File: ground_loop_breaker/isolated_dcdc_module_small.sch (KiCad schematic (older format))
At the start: 18 parts, among them J7 Conn_01x02_Male, J8 Conn_Coaxial, J9 Conn_01x02_Male

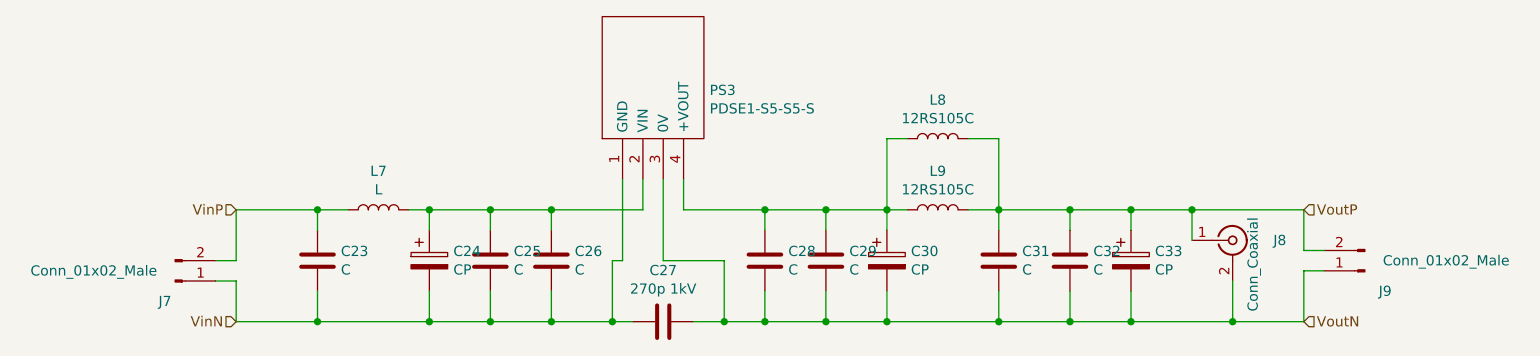
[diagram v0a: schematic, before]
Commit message: ground loop breaker fin
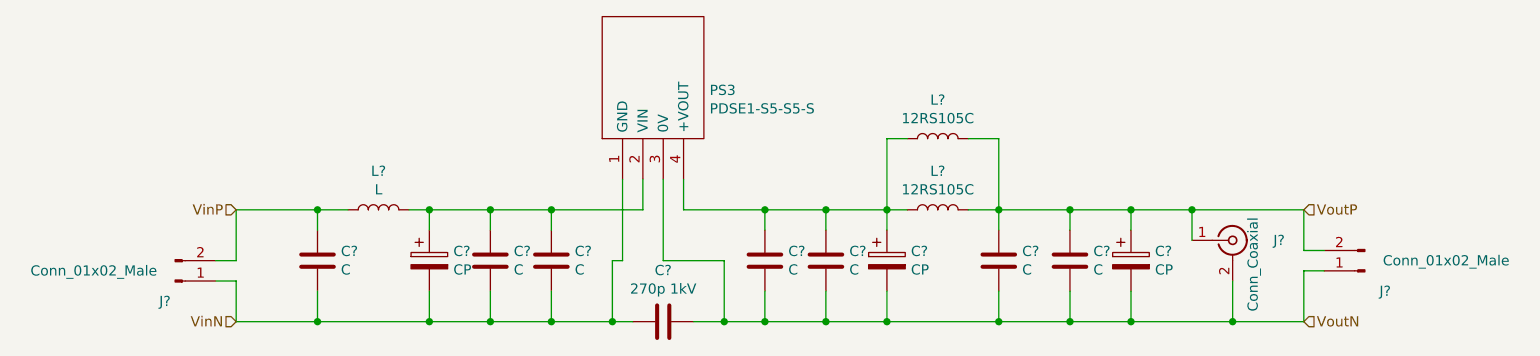
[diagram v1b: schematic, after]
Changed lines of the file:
@@
 $Descr A4 11693 8268
 encoding utf-8
-Sheet 4 5
+Sheet 3 5
 Title ""
 Date ""
@@
 AR Path="/613A5306/613A68CE" Ref="C26"  Part="1"
 AR Path="/613C5D0D/613A68CE" Ref="C?"  Part="1"
-F 0 "C26" H 4015 4146 50  0000 L CNN
+AR Path="/6135BAF1/613A68CE" Ref="C48"  Part="1"
+AR Path="/6135EEFA/613A68CE" Ref="C48"  Part="1"
+AR Path="/61365BC4/613A68CE" Ref="C?"  Part="1"
+F 0 "C?" H 4015 4146 50  0000 L CNN
 F 1 "C" H 4015 4055 50  0000 L CNN
 F 2 "SamacSys_Parts:C_1206_0805_dual" H 3938 3950 50  0001 C CNN
@@
 AR Path="/613A5306/613A68D4" Ref="C25"  Part="1"
 AR Path="/613C5D0D/613A68D4" Ref="C?"  Part="1"
-F 0 "C25" H 3715 4146 50  0000 L CNN
+AR Path="/6135BAF1/613A68D4" Ref="C47"  Part="1"
+AR Path="/6135EEFA/613A68D4" Ref="C47"  Part="1"
+AR Path="/61365BC4/613A68D4" Ref="C?"  Part="1"
+F 0 "C?" H 3715 4146 50  0000 L CNN
 F 1 "C" H 3715 4055 50  0000 L CNN
 F 2 "Capacitor_SMD:C_1206_3216Metric_Pad1.42x1.75mm_HandSolder" H 3638 3950 50  0001 C CNN
@@
 AR Path="/613A5306/613A68E2" Ref="C24"  Part="1"
 AR Path="/613C5D0D/613A68E2" Ref="C?"  Part="1"
-F 0 "C24" H 3418 4146 50  0000 L CNN
+AR Path="/6135BAF1/613A68E2" Ref="C46"  Part="1"
+AR Path="/6135EEFA/613A68E2" Ref="C46"  Part="1"
+AR Path="/61365BC4/613A68E2" Ref="C?"  Part="1"
+F 0 "C?" H 3418 4146 50  0000 L CNN
 F 1 "CP" H 3418 4055 50  0000 L CNN
 F 2 "SamacSys_Parts:CP_Radial_D8_P3.5_2.5" H 3338 3950 50  0001 C CNN
@@
 AR Path="/613A5306/613A68F0" Ref="C23"  Part="1"
 AR Path="/613C5D0D/613A68F0" Ref="C?"  Part="1"
-F 0 "C23" H 2865 4146 50  0000 L CNN
+AR Path="/6135BAF1/613A68F0" Ref="C45"  Part="1"
+AR Path="/6135EEFA/613A68F0" Ref="C45"  Part="1"
+AR Path="/61365BC4/613A68F0" Ref="C?"  Part="1"
+F 0 "C?" H 2865 4146 50  0000 L CNN
 F 1 "C" H 2865 4055 50  0000 L CNN
 F 2 "Capacitor_SMD:C_1206_3216Metric_Pad1.42x1.75mm_HandSolder" H 2788 3950 50  0001 C CNN
@@
 AR Path="/613A5306/613A68F6" Ref="L7"  Part="1"
 AR Path="/613C5D0D/613A68F6" Ref="L?"  Part="1"
-F 0 "L7" V 3240 3850 50  0000 C CNN
+AR Path="/6135BAF1/613A68F6" Ref="L13"  Part="1"
+AR Path="/6135EEFA/613A68F6" Ref="L13"  Part="1"
+AR Path="/61365BC4/613A68F6" Ref="L?"  Part="1"
+F 0 "L?" V 3240 3850 50  0000 C CNN
 F 1 "L" V 3149 3850 50  0000 C CNN
 F 2 "Inductor_SMD:L_Bourns-SRN4018" H 3050 3850 50  0001 C CNN
@@
 AR Path="/613A5306/613A68FF" Ref="C29"  Part="1"
 AR Path="/613C5D0D/613A68FF" Ref="C?"  Part="1"
-F 0 "C29" H 5365 4146 50  0000 L CNN
+AR Path="/6135BAF1/613A68FF" Ref="C51"  Part="1"
+AR Path="/6135EEFA/613A68FF" Ref="C51"  Part="1"
+AR Path="/61365BC4/613A68FF" Ref="C?"  Part="1"
+F 0 "C?" H 5365 4146 50  0000 L CNN
 F 1 "C" H 5365 4055 50  0000 L CNN
 F 2 "Capacitor_SMD:C_1206_3216Metric_Pad1.42x1.75mm_HandSolder" H 5288 3950 50  0001 C CNN
@@
 AR Path="/613A5306/613A6915" Ref="C31"  Part="1"
 AR Path="/613C5D0D/613A6915" Ref="C?"  Part="1"
-F 0 "C31" H 6215 4146 50  0000 L CNN
+AR Path="/6135BAF1/613A6915" Ref="C53"  Part="1"
+AR Path="/6135EEFA/613A6915" Ref="C53"  Part="1"
+AR Path="/61365BC4/613A6915" Ref="C?"  Part="1"
+F 0 "C?" H 6215 4146 50  0000 L CNN
 F 1 "C" H 6215 4055 50  0000 L CNN
 F 2 "Capacitor_SMD:C_1206_3216Metric_Pad1.42x1.75mm_HandSolder" H 6138 3950 50  0001 C CNN
@@
 AR Path="/613A5306/613A691B" Ref="L9"  Part="1"
 AR Path="/613C5D0D/613A691B" Ref="L?"  Part="1"
-F 0 "L9" V 5990 3850 50  0000 C CNN
+AR Path="/6135BAF1/613A691B" Ref="L15"  Part="1"
+AR Path="/6135EEFA/613A691B" Ref="L15"  Part="1"
+AR Path="/61365BC4/613A691B" Ref="L?"  Part="1"
+F 0 "L?" V 5990 3850 50  0000 C CNN
 F 1 "12RS105C" V 5899 3850 50  0000 C CNN
 F 2 "Inductor_THT:L_Radial_D10.5mm_P4.00x5.00mm_Murata_1200RS" H 5800 3850 50  0001 C CNN
@@
 AR Path="/613A5306/613A6922" Ref="C28"  Part="1"
 AR Path="/613C5D0D/613A6922" Ref="C?"  Part="1"
-F 0 "C28" H 5065 4146 50  0000 L CNN
+AR Path="/6135BAF1/613A6922" Ref="C50"  Part="1"
+AR Path="/6135EEFA/613A6922" Ref="C50"  Part="1"
+AR Path="/61365BC4/613A6922" Ref="C?"  Part="1"
+F 0 "C?" H 5065 4146 50  0000 L CNN
 F 1 "C" H 5065 4055 50  0000 L CNN
 F 2 "SamacSys_Parts:C_1206_0805_dual" H 4988 3950 50  0001 C CNN
@@
 AR Path="/613A5306/613A6928" Ref="C32"  Part="1"
 AR Path="/613C5D0D/613A6928" Ref="C?"  Part="1"
-F 0 "C32" H 6565 4146 50  0000 L CNN
+AR Path="/6135BAF1/613A6928" Ref="C54"  Part="1"
+AR Path="/6135EEFA/613A6928" Ref="C54"  Part="1"
+AR Path="/61365BC4/613A6928" Ref="C?"  Part="1"
+F 0 "C?" H 6565 4146 50  0000 L CNN
 F 1 "C" H 6565 4055 50  0000 L CNN
 F 2 "Capacitor_SMD:C_1206_3216Metric_Pad1.42x1.75mm_HandSolder" H 6488 3950 50  0001 C CNN
@@
 AR Path="/613A5306/613A692E" Ref="C33"  Part="1"
 AR Path="/613C5D0D/613A692E" Ref="C?"  Part="1"
-F 0 "C33" H 6868 4146 50  0000 L CNN
+AR Path="/6135BAF1/613A692E" Ref="C55"  Part="1"
+AR Path="/6135EEFA/613A692E" Ref="C55"  Part="1"
+AR Path="/61365BC4/613A692E" Ref="C?"  Part="1"
+F 0 "C?" H 6868 4146 50  0000 L CNN
 F 1 "CP" H 6868 4055 50  0000 L CNN
 F 2 "SamacSys_Parts:CP_Radial_D10.0mm_P3.5_5" H 6788 3950 50  0001 C CNN
@@
 AR Path="/613A5306/613A6940" Ref="C30"  Part="1"
 AR Path="/613C5D0D/613A6940" Ref="C?"  Part="1"
-F 0 "C30" H 5668 4146 50  0000 L CNN
+AR Path="/6135BAF1/613A6940" Ref="C52"  Part="1"
+AR Path="/6135EEFA/613A6940" Ref="C52"  Part="1"
+AR Path="/61365BC4/613A6940" Ref="C?"  Part="1"
+F 0 "C?" H 5668 4146 50  0000 L CNN
 F 1 "CP" H 5668 4055 50  0000 L CNN
 F 2 "SamacSys_Parts:CP_Radial_D8_P3.5_2.5" H 5588 3950 50  0001 C CNN
@@
 AR Path="/613A5306/613A6946" Ref="J7"  Part="1"
 AR Path="/613C5D0D/613A6946" Ref="J?"  Part="1"
-F 0 "J7" H 2000 4300 50  0000 C CNN
+AR Path="/6135BAF1/613A6946" Ref="J13"  Part="1"
+AR Path="/6135EEFA/613A6946" Ref="J13"  Part="1"
+AR Path="/61365BC4/613A6946" Ref="J?"  Part="1"
+F 0 "J?" H 2000 4300 50  0000 C CNN
 F 1 "Conn_01x02_Male" H 1650 4150 50  0000 C CNN
 F 2 "Connector_PinHeader_2.54mm:PinHeader_1x02_P2.54mm_Vertical" H 2050 4200 50  0001 C CNN
@@
 AR Path="/613A5306/613A6954" Ref="J9"  Part="1"
 AR Path="/613C5D0D/613A6954" Ref="J?"  Part="1"
-F 0 "J9" H 7800 4250 50  0000 C CNN
+AR Path="/6135BAF1/613A6954" Ref="J15"  Part="1"
+AR Path="/6135EEFA/613A6954" Ref="J15"  Part="1"
+AR Path="/61365BC4/613A6954" Ref="J?"  Part="1"
+F 0 "J?" H 7800 4250 50  0000 C CNN
 F 1 "Conn_01x02_Male" H 7500 4100 50  0000 C CNN
 F 2 "Connector_PinHeader_2.54mm:PinHeader_1x02_P2.54mm_Vertical" H 7900 4150 50  0001 C CNN
@@
 AR Path="/613A5306/613A6971" Ref="L8"  Part="1"
 AR Path="/613C5D0D/613A6971" Ref="L?"  Part="1"
-F 0 "L8" V 5990 3500 50  0000 C CNN
+AR Path="/6135BAF1/613A6971" Ref="L14"  Part="1"
+AR Path="/6135EEFA/613A6971" Ref="L14"  Part="1"
+AR Path="/61365BC4/613A6971" Ref="L?"  Part="1"
+F 0 "L?" V 5990 3500 50  0000 C CNN
 F 1 "12RS105C" V 5899 3500 50  0000 C CNN
 F 2 "Inductor_THT:L_Radial_D10.0mm_P5.00mm_Fastron_07P" H 5800 3500 50  0001 C CNN
@@
 AR Path="/613A5306/613A697B" Ref="C27"  Part="1"
 AR Path="/613C5D0D/613A697B" Ref="C?"  Part="1"
-F 0 "C27" V 4198 4400 50  0000 C CNN
+AR Path="/6135BAF1/613A697B" Ref="C49"  Part="1"
+AR Path="/6135EEFA/613A697B" Ref="C49"  Part="1"
+AR Path="/61365BC4/613A697B" Ref="C?"  Part="1"
+F 0 "C?" V 4198 4400 50  0000 C CNN
 F 1 "270p 1kV" V 4289 4400 50  0000 C CNN
 F 2 "Capacitor_SMD:C_1206_3216Metric_Pad1.42x1.75mm_HandSolder" H 4488 4250 50  0001 C CNN
@@
 AR Path="/613A5306/613A6993" Ref="J8"  Part="1"
 AR Path="/613C5D0D/613A6993" Ref="J?"  Part="1"
-F 0 "J8" H 7450 4000 50  0000 L CNN
+AR Path="/6135BAF1/613A6993" Ref="J14"  Part="1"
+AR Path="/6135EEFA/613A6993" Ref="J14"  Part="1"
+AR Path="/61365BC4/613A6993" Ref="J?"  Part="1"
+F 0 "J?" H 7450 4000 50  0000 L CNN
 F 1 "Conn_Coaxial" V 7350 3650 50  0000 L CNN
 F 2 "Connector_Coaxial:U.FL_Hirose_U.FL-R-SMT-1_Vertical" H 7250 4000 50  0001 C CNN
@@
 AR Path="/613A5306/613AC1D6" Ref="PS3"  Part="1"
 AR Path="/613C5D0D/613AC1D6" Ref="PS?"  Part="1"
-F 0 "PS3" V 4688 3272 50  0000 R CNN
+AR Path="/6135BAF1/613AC1D6" Ref="PS5"  Part="1"
+AR Path="/6135EEFA/613AC1D6" Ref="PS5"  Part="1"
+AR Path="/61365BC4/613AC1D6" Ref="PS?"  Part="1"
+F 0 "PS?" V 4688 3272 50  0000 R CNN
 F 1 "PDSE1-S5-S5-S" V 4597 3272 50  0000 R CNN
 F 2 "PDSE1S5S5S" H 5100 3800 50  0001 L CNN

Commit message: Relay array board; Last checkup; Gerberfile updates
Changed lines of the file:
@@
 $Descr A4 11693 8268
 encoding utf-8
-Sheet 3 5
+Sheet 3 6
 Title ""
 Date ""
@@
 AR Path="/6135BAF1/613A68CE" Ref="C48"  Part="1"
 AR Path="/6135EEFA/613A68CE" Ref="C48"  Part="1"
-AR Path="/61365BC4/613A68CE" Ref="C?"  Part="1"
-F 0 "C?" H 4015 4146 50  0000 L CNN
+AR Path="/61365BC4/613A68CE" Ref="C48"  Part="1"
+F 0 "C26" H 4015 4146 50  0000 L CNN
 F 1 "C" H 4015 4055 50  0000 L CNN
 F 2 "SamacSys_Parts:C_1206_0805_dual" H 3938 3950 50  0001 C CNN
@@
 AR Path="/6135BAF1/613A68D4" Ref="C47"  Part="1"
 AR Path="/6135EEFA/613A68D4" Ref="C47"  Part="1"
-AR Path="/61365BC4/613A68D4" Ref="C?"  Part="1"
-F 0 "C?" H 3715 4146 50  0000 L CNN
+AR Path="/61365BC4/613A68D4" Ref="C47"  Part="1"
+F 0 "C25" H 3715 4146 50  0000 L CNN
 F 1 "C" H 3715 4055 50  0000 L CNN
 F 2 "Capacitor_SMD:C_1206_3216Metric_Pad1.42x1.75mm_HandSolder" H 3638 3950 50  0001 C CNN
@@
 AR Path="/6135BAF1/613A68E2" Ref="C46"  Part="1"
 AR Path="/6135EEFA/613A68E2" Ref="C46"  Part="1"
-AR Path="/61365BC4/613A68E2" Ref="C?"  Part="1"
-F 0 "C?" H 3418 4146 50  0000 L CNN
+AR Path="/61365BC4/613A68E2" Ref="C46"  Part="1"
+F 0 "C24" H 3418 4146 50  0000 L CNN
 F 1 "CP" H 3418 4055 50  0000 L CNN
 F 2 "SamacSys_Parts:CP_Radial_D8_P3.5_2.5" H 3338 3950 50  0001 C CNN
@@
 AR Path="/6135BAF1/613A68F0" Ref="C45"  Part="1"
 AR Path="/6135EEFA/613A68F0" Ref="C45"  Part="1"
-AR Path="/61365BC4/613A68F0" Ref="C?"  Part="1"
-F 0 "C?" H 2865 4146 50  0000 L CNN
+AR Path="/61365BC4/613A68F0" Ref="C45"  Part="1"
+F 0 "C23" H 2865 4146 50  0000 L CNN
 F 1 "C" H 2865 4055 50  0000 L CNN
 F 2 "Capacitor_SMD:C_1206_3216Metric_Pad1.42x1.75mm_HandSolder" H 2788 3950 50  0001 C CNN
@@
 AR Path="/6135BAF1/613A68F6" Ref="L13"  Part="1"
 AR Path="/6135EEFA/613A68F6" Ref="L13"  Part="1"
-AR Path="/61365BC4/613A68F6" Ref="L?"  Part="1"
-F 0 "L?" V 3240 3850 50  0000 C CNN
+AR Path="/61365BC4/613A68F6" Ref="L13"  Part="1"
+F 0 "L7" V 3240 3850 50  0000 C CNN
 F 1 "L" V 3149 3850 50  0000 C CNN
 F 2 "Inductor_SMD:L_Bourns-SRN4018" H 3050 3850 50  0001 C CNN
@@
 AR Path="/6135BAF1/613A68FF" Ref="C51"  Part="1"
 AR Path="/6135EEFA/613A68FF" Ref="C51"  Part="1"
-AR Path="/61365BC4/613A68FF" Ref="C?"  Part="1"
-F 0 "C?" H 5365 4146 50  0000 L CNN
+AR Path="/61365BC4/613A68FF" Ref="C51"  Part="1"
+F 0 "C29" H 5365 4146 50  0000 L CNN
 F 1 "C" H 5365 4055 50  0000 L CNN
 F 2 "Capacitor_SMD:C_1206_3216Metric_Pad1.42x1.75mm_HandSolder" H 5288 3950 50  0001 C CNN
@@
 AR Path="/6135BAF1/613A6915" Ref="C53"  Part="1"
 AR Path="/6135EEFA/613A6915" Ref="C53"  Part="1"
-AR Path="/61365BC4/613A6915" Ref="C?"  Part="1"
-F 0 "C?" H 6215 4146 50  0000 L CNN
+AR Path="/61365BC4/613A6915" Ref="C53"  Part="1"
+F 0 "C31" H 6215 4146 50  0000 L CNN
 F 1 "C" H 6215 4055 50  0000 L CNN
 F 2 "Capacitor_SMD:C_1206_3216Metric_Pad1.42x1.75mm_HandSolder" H 6138 3950 50  0001 C CNN
@@
 AR Path="/6135BAF1/613A691B" Ref="L15"  Part="1"
 AR Path="/6135EEFA/613A691B" Ref="L15"  Part="1"
-AR Path="/61365BC4/613A691B" Ref="L?"  Part="1"
-F 0 "L?" V 5990 3850 50  0000 C CNN
+AR Path="/61365BC4/613A691B" Ref="L15"  Part="1"
+F 0 "L9" V 5990 3850 50  0000 C CNN
 F 1 "12RS105C" V 5899 3850 50  0000 C CNN
 F 2 "Inductor_THT:L_Radial_D10.5mm_P4.00x5.00mm_Murata_1200RS" H 5800 3850 50  0001 C CNN
@@
 AR Path="/6135BAF1/613A6922" Ref="C50"  Part="1"
 AR Path="/6135EEFA/613A6922" Ref="C50"  Part="1"
-AR Path="/61365BC4/613A6922" Ref="C?"  Part="1"
-F 0 "C?" H 5065 4146 50  0000 L CNN
+AR Path="/61365BC4/613A6922" Ref="C50"  Part="1"
+F 0 "C28" H 5065 4146 50  0000 L CNN
 F 1 "C" H 5065 4055 50  0000 L CNN
 F 2 "SamacSys_Parts:C_1206_0805_dual" H 4988 3950 50  0001 C CNN
@@
 AR Path="/6135BAF1/613A6928" Ref="C54"  Part="1"
 AR Path="/6135EEFA/613A6928" Ref="C54"  Part="1"
-AR Path="/61365BC4/613A6928" Ref="C?"  Part="1"
-F 0 "C?" H 6565 4146 50  0000 L CNN
+AR Path="/61365BC4/613A6928" Ref="C54"  Part="1"
+F 0 "C32" H 6565 4146 50  0000 L CNN
 F 1 "C" H 6565 4055 50  0000 L CNN
 F 2 "Capacitor_SMD:C_1206_3216Metric_Pad1.42x1.75mm_HandSolder" H 6488 3950 50  0001 C CNN
@@
 AR Path="/6135BAF1/613A692E" Ref="C55"  Part="1"
 AR Path="/6135EEFA/613A692E" Ref="C55"  Part="1"
-AR Path="/61365BC4/613A692E" Ref="C?"  Part="1"
-F 0 "C?" H 6868 4146 50  0000 L CNN
+AR Path="/61365BC4/613A692E" Ref="C55"  Part="1"
+F 0 "C33" H 6868 4146 50  0000 L CNN
 F 1 "CP" H 6868 4055 50  0000 L CNN
 F 2 "SamacSys_Parts:CP_Radial_D10.0mm_P3.5_5" H 6788 3950 50  0001 C CNN
@@
 AR Path="/6135BAF1/613A6940" Ref="C52"  Part="1"
 AR Path="/6135EEFA/613A6940" Ref="C52"  Part="1"
-AR Path="/61365BC4/613A6940" Ref="C?"  Part="1"
-F 0 "C?" H 5668 4146 50  0000 L CNN
+AR Path="/61365BC4/613A6940" Ref="C52"  Part="1"
+F 0 "C30" H 5668 4146 50  0000 L CNN
 F 1 "CP" H 5668 4055 50  0000 L CNN
 F 2 "SamacSys_Parts:CP_Radial_D8_P3.5_2.5" H 5588 3950 50  0001 C CNN
@@
 AR Path="/6135BAF1/613A6946" Ref="J13"  Part="1"
 AR Path="/6135EEFA/613A6946" Ref="J13"  Part="1"
-AR Path="/61365BC4/613A6946" Ref="J?"  Part="1"
-F 0 "J?" H 2000 4300 50  0000 C CNN
+AR Path="/61365BC4/613A6946" Ref="J13"  Part="1"
+F 0 "J7" H 2000 4300 50  0000 C CNN
 F 1 "Conn_01x02_Male" H 1650 4150 50  0000 C CNN
 F 2 "Connector_PinHeader_2.54mm:PinHeader_1x02_P2.54mm_Vertical" H 2050 4200 50  0001 C CNN
@@
 AR Path="/6135BAF1/613A6954" Ref="J15"  Part="1"
 AR Path="/6135EEFA/613A6954" Ref="J15"  Part="1"
-AR Path="/61365BC4/613A6954" Ref="J?"  Part="1"
-F 0 "J?" H 7800 4250 50  0000 C CNN
+AR Path="/61365BC4/613A6954" Ref="J15"  Part="1"
+F 0 "J9" H 7800 4250 50  0000 C CNN
 F 1 "Conn_01x02_Male" H 7500 4100 50  0000 C CNN
 F 2 "Connector_PinHeader_2.54mm:PinHeader_1x02_P2.54mm_Vertical" H 7900 4150 50  0001 C CNN
@@
 AR Path="/6135BAF1/613A6971" Ref="L14"  Part="1"
 AR Path="/6135EEFA/613A6971" Ref="L14"  Part="1"
-AR Path="/61365BC4/613A6971" Ref="L?"  Part="1"
-F 0 "L?" V 5990 3500 50  0000 C CNN
+AR Path="/61365BC4/613A6971" Ref="L14"  Part="1"
+F 0 "L8" V 5990 3500 50  0000 C CNN
 F 1 "12RS105C" V 5899 3500 50  0000 C CNN
 F 2 "Inductor_THT:L_Radial_D10.0mm_P5.00mm_Fastron_07P" H 5800 3500 50  0001 C CNN
@@
 AR Path="/6135BAF1/613A697B" Ref="C49"  Part="1"
 AR Path="/6135EEFA/613A697B" Ref="C49"  Part="1"
-AR Path="/61365BC4/613A697B" Ref="C?"  Part="1"
-F 0 "C?" V 4198 4400 50  0000 C CNN
+AR Path="/61365BC4/613A697B" Ref="C49"  Part="1"
+F 0 "C27" V 4198 4400 50  0000 C CNN
 F 1 "270p 1kV" V 4289 4400 50  0000 C CNN
 F 2 "Capacitor_SMD:C_1206_3216Metric_Pad1.42x1.75mm_HandSolder" H 4488 4250 50  0001 C CNN
@@
 AR Path="/6135BAF1/613A6993" Ref="J14"  Part="1"
 AR Path="/6135EEFA/613A6993" Ref="J14"  Part="1"
-AR Path="/61365BC4/613A6993" Ref="J?"  Part="1"
-F 0 "J?" H 7450 4000 50  0000 L CNN
+AR Path="/61365BC4/613A6993" Ref="J14"  Part="1"
+F 0 "J8" H 7450 4000 50  0000 L CNN
 F 1 "Conn_Coaxial" V 7350 3650 50  0000 L CNN
 F 2 "Connector_Coaxial:U.FL_Hirose_U.FL-R-SMT-1_Vertical" H 7250 4000 50  0001 C CNN
@@
 AR Path="/6135BAF1/613AC1D6" Ref="PS5"  Part="1"
 AR Path="/6135EEFA/613AC1D6" Ref="PS5"  Part="1"
-AR Path="/61365BC4/613AC1D6" Ref="PS?"  Part="1"
-F 0 "PS?" V 4688 3272 50  0000 R CNN
+AR Path="/61365BC4/613AC1D6" Ref="PS5"  Part="1"
+F 0 "PS3" V 4688 3272 50  0000 R CNN
 F 1 "PDSE1-S5-S5-S" V 4597 3272 50  0000 R CNN
 F 2 "PDSE1S5S5S" H 5100 3800 50  0001 L CNN
